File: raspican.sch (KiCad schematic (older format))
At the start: 17 parts, among them J2 CONN_01X06, P1 CONN_13X2, SW1 BUTTON_FRAME, SW2 BUTTON_FRAME, U4 MCP2515, Y1 16MHz

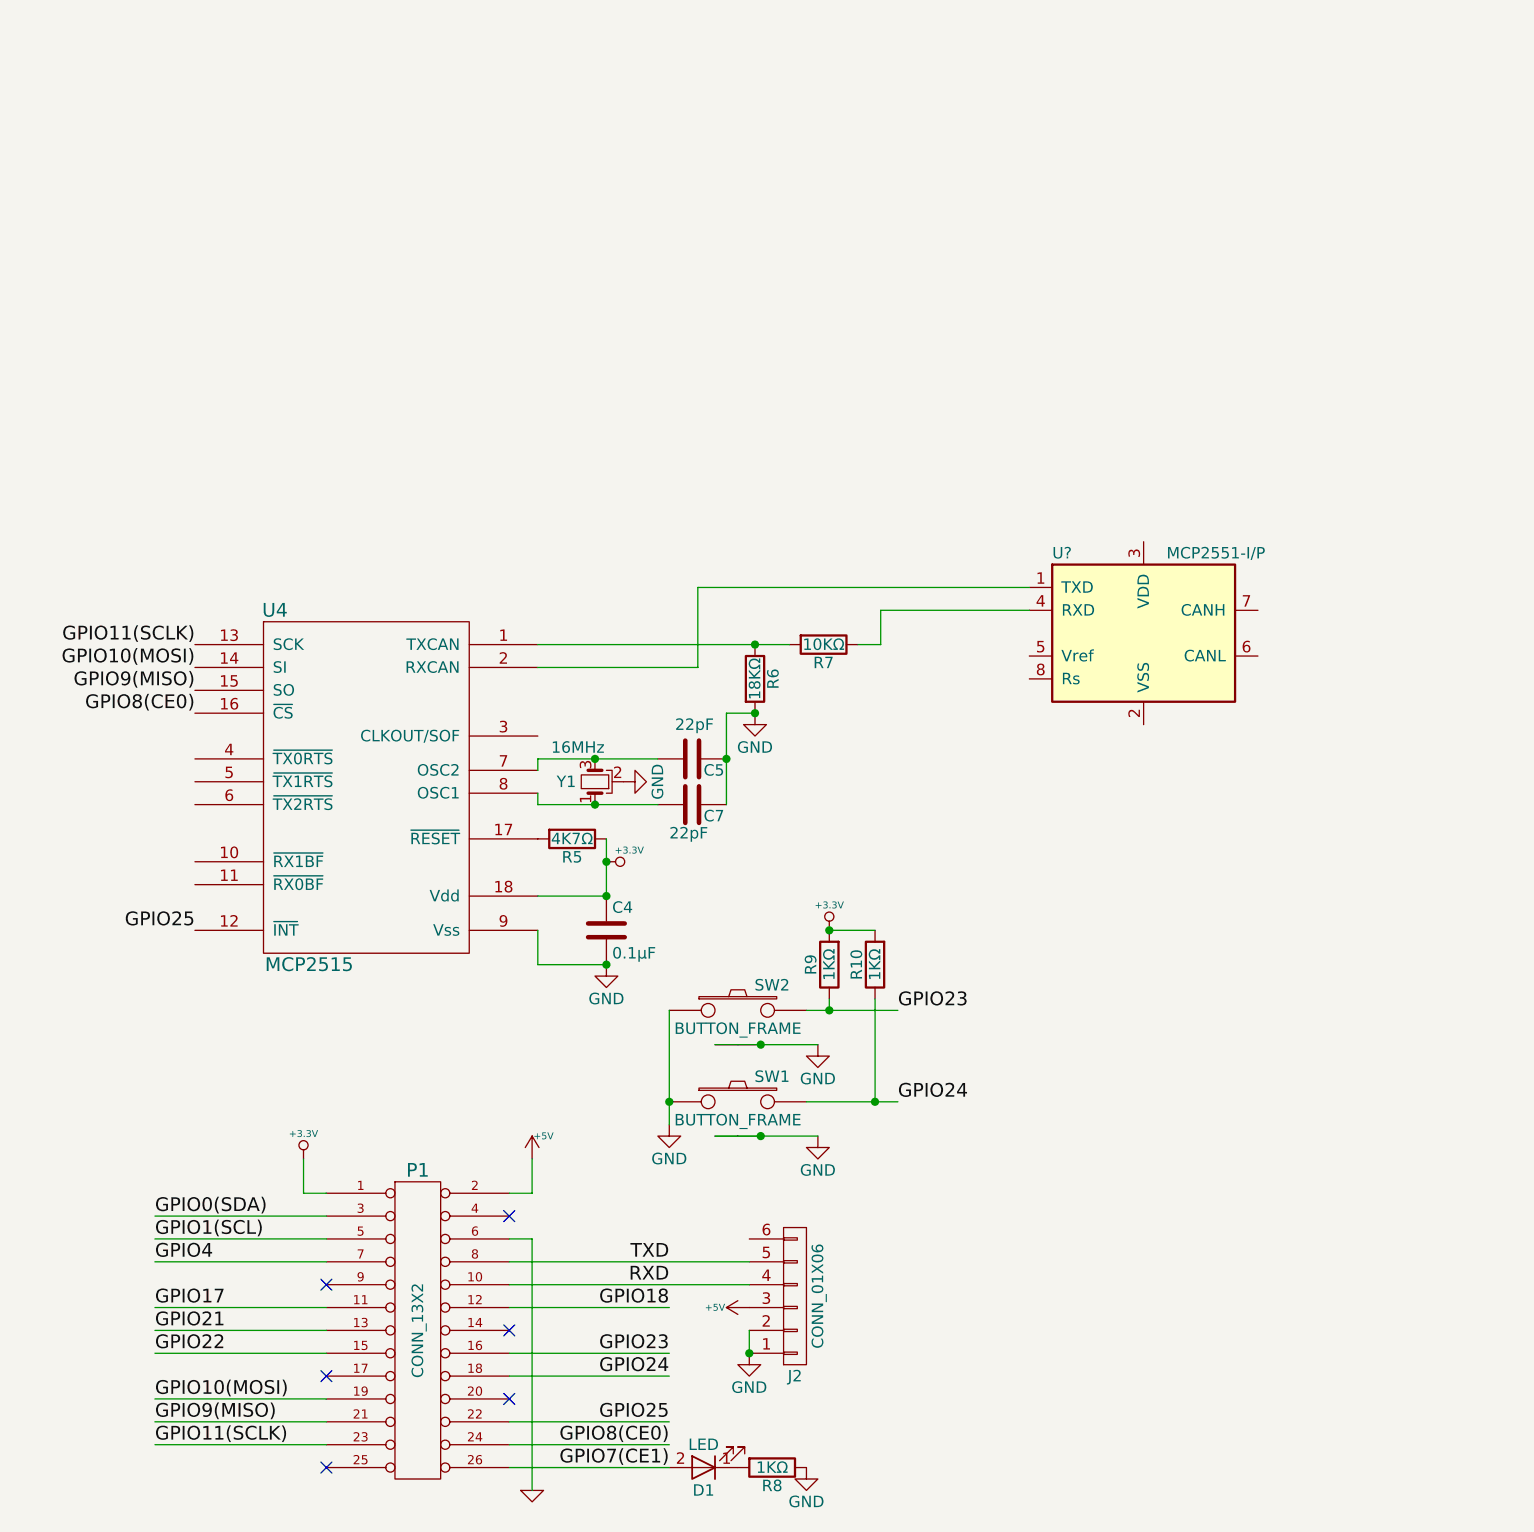
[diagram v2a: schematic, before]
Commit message: finished schematic, ready to make a board
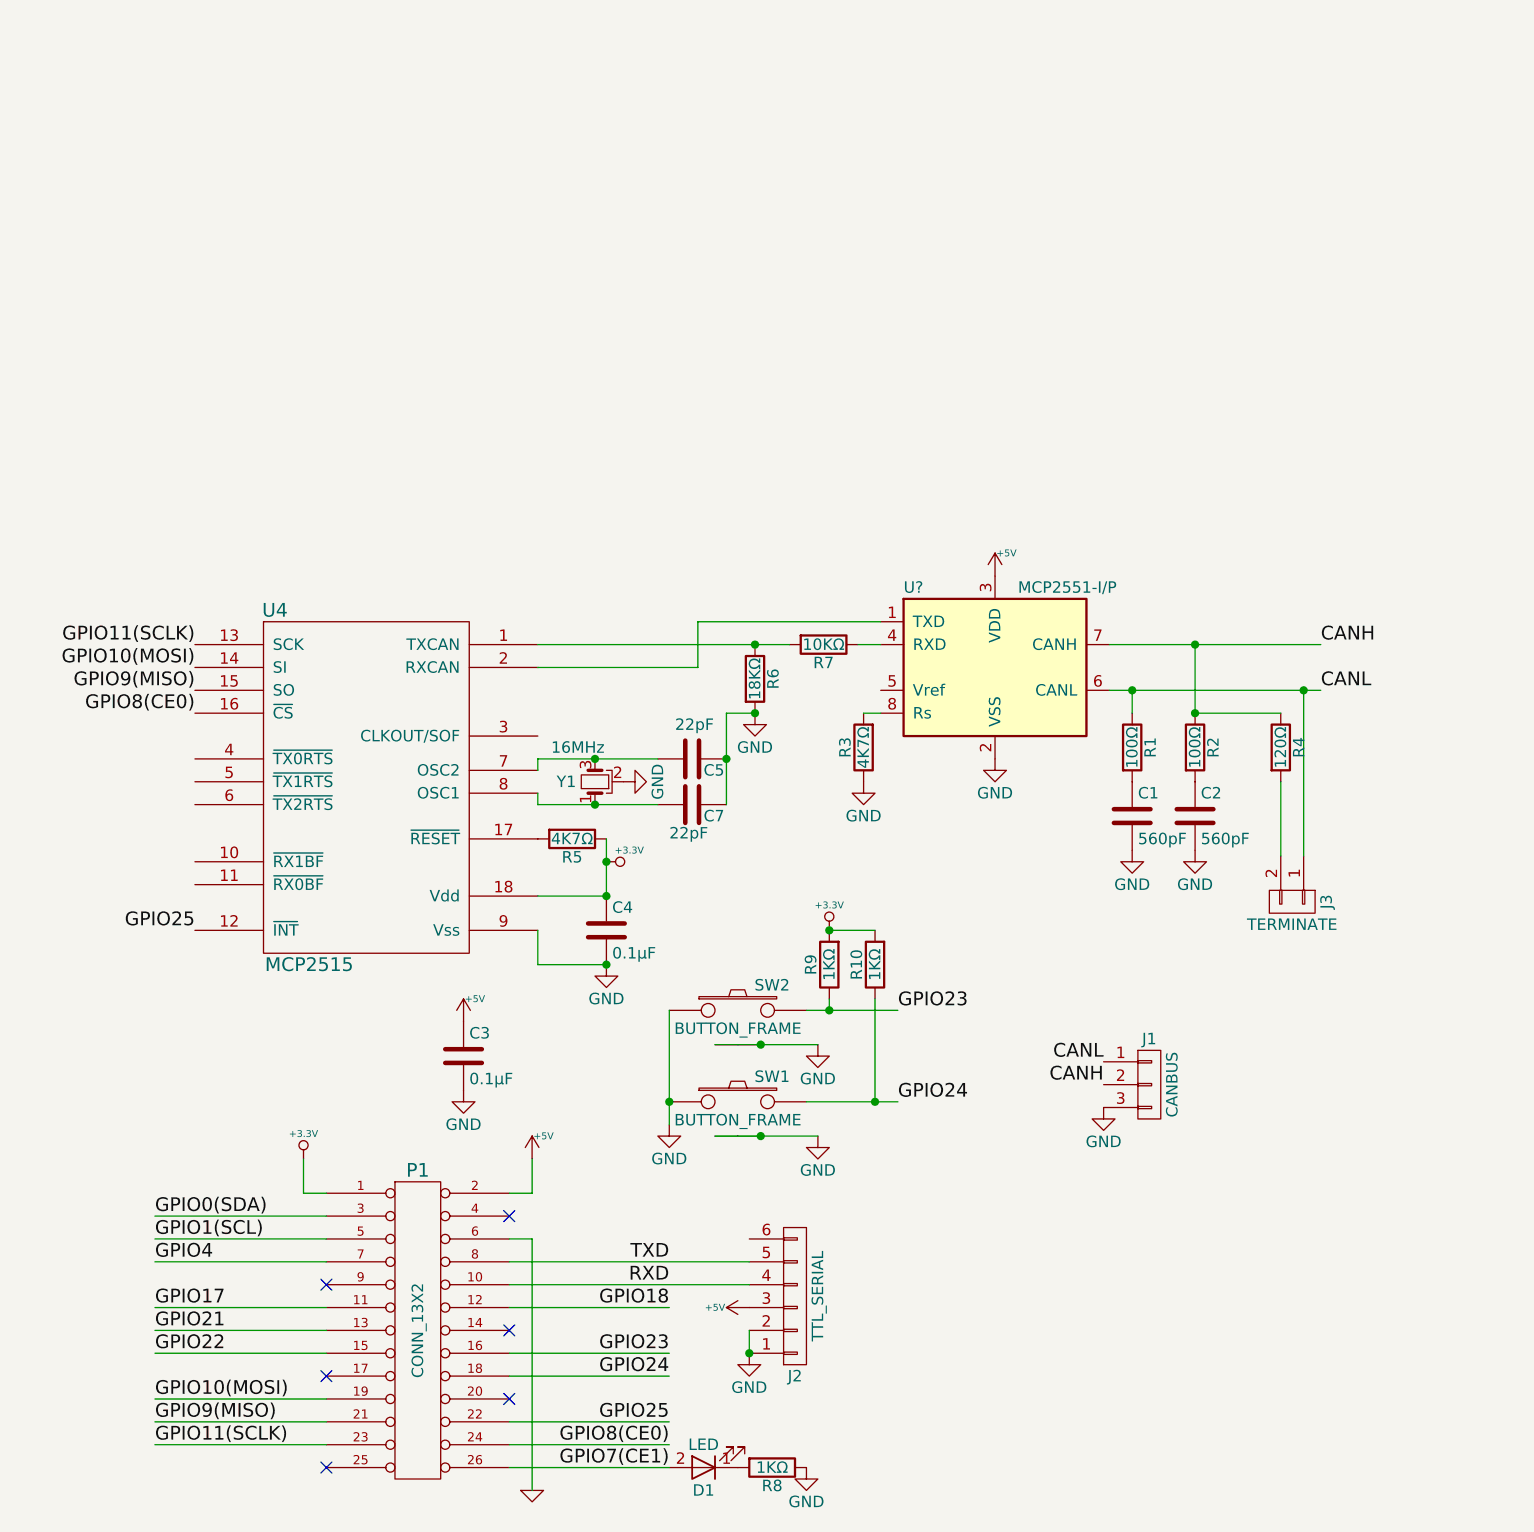
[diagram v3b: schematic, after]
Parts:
- added C1, C2: 560pF, symbol C
- added C3: 0.1μF, symbol C
- added J1: CANBUS, symbol CONN_01X03
- added J3: TERMINATE, symbol CONN_01X02
- added R1, R2: 100Ω, symbol R
- added R3: 4K7Ω, symbol R
- added R4: 120Ω, symbol R
- J2: value CONN_01X06 -> TTL_SERIAL
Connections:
- net +5V: now also U?.3 (VDD), C3.1
- net GND: now also U?.2 (VSS), C1.2, C2.2, C3.2, J1.3 (P3), R3.1
- net CANL: now reaches U?.6 (CANL)
- net CANL: now also J1.1 (P1), J3.1 (P1), R1.1
- net CANH: now reaches U?.7 (CANH)
- net CANH: now also J1.2 (P2), R2.1, R4.1
- net at U?.8 (Rs): now also R3.2
- new net: C1.1, R1.2
- new net: C2.1, R2.2
- new net: J3.2 (P2), R4.2
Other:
- moved on the sheet: U?
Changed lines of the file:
@@
 L MCP2551-I/P U?
 U 1 1 58B8BB6A
-P 5575 3600
-F 0 "U?" H 5175 3950 50  0000 L CNN
-F 1 "MCP2551-I/P" H 5675 3950 50  0000 L CNN
-F 2 "Housings_DIP:DIP-8_W7.62mm" H 5575 3100 50  0001 C CIN
-F 3 "" H 5575 3600 50  0001 C CNN
-	1    5575 3600
+P 4925 3750
+F 0 "U?" H 4525 4100 50  0000 L CNN
+F 1 "MCP2551-I/P" H 5025 4100 50  0000 L CNN
+F 2 "Housings_DIP:DIP-8_W7.62mm" H 4925 3250 50  0001 C CIN
+F 3 "" H 4925 3750 50  0001 C CNN
+	1    4925 3750
 	1    0    0    -1
 $EndComp
@@
 P 4050 6500
 F 0 "J2" H 4050 6850 50  0000 C CNN
-F 1 "CONN_01X06" V 4150 6500 50  0000 C CNN
+F 1 "TTL_SERIAL" V 4150 6500 50  0000 C CNN
 F 2 "" H 4050 6500 50  0001 C CNN
 F 3 "" H 4050 6500 50  0001 C CNN
@@
 Wire Wire Line
 	2925 3750 3625 3750
-Wire Wire Line
-	3625 3750 3625 3400
-Wire Wire Line
-	3625 3400 5075 3400
 $Comp
 L R R7
@@
 Wire Wire Line
 	4325 3650 4425 3650
-Wire Wire Line
-	4425 3650 4425 3500
-Wire Wire Line
-	4425 3500 5075 3500
 $Comp
 L R R6
@@
 Text Label 1425 3650 2    60   ~ 0
 GPIO11(SCLK)
+$Comp
+L +5V #PWR?
+U 1 1 58BA15CD
+P 4925 3350
+F 0 "#PWR?" H 4925 3440 20  0001 C CNN
+F 1 "+5V" H 4975 3450 30  0000 C CNN
+F 2 "" H 4925 3350 60  0001 C CNN
+F 3 "" H 4925 3350 60  0001 C CNN
+	1    4925 3350
+	1    0    0    -1
+$EndComp
+$Comp
+L C C3
+U 1 1 58BA1693
+P 2600 5450
+F 0 "C3" H 2625 5550 50  0000 L CNN
+F 1 "0.1μF" H 2625 5350 50  0000 L CNN
+F 2 "" H 2638 5300 50  0001 C CNN
+F 3 "" H 2600 5450 50  0001 C CNN
+	1    2600 5450
+	1    0    0    -1
+$EndComp
+$Comp
+L GND #PWR?
+U 1 1 58BA19FF
+P 2600 5600
+F 0 "#PWR?" H 2600 5350 50  0001 C CNN
+F 1 "GND" H 2600 5450 50  0000 C CNN
+F 2 "" H 2600 5600 50  0001 C CNN
+F 3 "" H 2600 5600 50  0001 C CNN
+	1    2600 5600
+	1    0    0    -1
+$EndComp
+$Comp
+L +5V #PWR?
+U 1 1 58BA1B7F
+P 2600 5300
+F 0 "#PWR?" H 2600 5390 20  0001 C CNN
+F 1 "+5V" H 2650 5400 30  0000 C CNN
+F 2 "" H 2600 5300 60  0001 C CNN
+F 3 "" H 2600 5300 60  0001 C CNN
+	1    2600 5300
+	1    0    0    -1
+$EndComp
+$Comp
+L GND #PWR?
+U 1 1 58BA1C71
+P 4925 4150
+F 0 "#PWR?" H 4925 3900 50  0001 C CNN
+F 1 "GND" H 4925 4000 50  0000 C CNN
+F 2 "" H 4925 4150 50  0001 C CNN
+F 3 "" H 4925 4150 50  0001 C CNN
+	1    4925 4150
+	1    0    0    -1
+$EndComp
+$Comp
+L R R3
+U 1 1 58BA1CB2
+P 4350 4100
+F 0 "R3" V 4430 4100 50  0000 C CNN
+F 1 "4K7Ω" V 4350 4100 50  0000 C CNN
+F 2 "" V 4280 4100 50  0001 C CNN
+F 3 "" H 4350 4100 50  0001 C CNN
+	1    4350 4100
+	-1   0    0    1
+$EndComp
+Wire Wire Line
+	4350 3950 4425 3950
+$Comp
+L GND #PWR?
+U 1 1 58BA1E42
+P 4350 4250
+F 0 "#PWR?" H 4350 4000 50  0001 C CNN
+F 1 "GND" H 4350 4100 50  0000 C CNN
+F 2 "" H 4350 4250 50  0001 C CNN
+F 3 "" H 4350 4250 50  0001 C CNN
+	1    4350 4250
+	1    0    0    -1
+$EndComp
+$Comp
+L R R1
+U 1 1 58BA1E7C
+P 5525 4100
+F 0 "R1" V 5605 4100 50  0000 C CNN
+F 1 "100Ω" V 5525 4100 50  0000 C CNN
+F 2 "" V 5455 4100 50  0001 C CNN
+F 3 "" H 5525 4100 50  0001 C CNN
+	1    5525 4100
+	1    0    0    -1
+$EndComp
+$Comp
+L R R2
+U 1 1 58BA1F70
+P 5800 4100
+F 0 "R2" V 5880 4100 50  0000 C CNN
+F 1 "100Ω" V 5800 4100 50  0000 C CNN
+F 2 "" V 5730 4100 50  0001 C CNN
+F 3 "" H 5800 4100 50  0001 C CNN
+	1    5800 4100
+	1    0    0    -1
+$EndComp
+$Comp
+L C C2
+U 1 1 58BA1FBE
+P 5800 4400
+F 0 "C2" H 5825 4500 50  0000 L CNN
+F 1 "560pF" H 5825 4300 50  0000 L CNN
+F 2 "" H 5838 4250 50  0001 C CNN
+F 3 "" H 5800 4400 50  0001 C CNN
+	1    5800 4400
+	1    0    0    -1
+$EndComp
+$Comp
+L C C1
+U 1 1 58BA204E
+P 5525 4400
+F 0 "C1" H 5550 4500 50  0000 L CNN
+F 1 "560pF" H 5550 4300 50  0000 L CNN
+F 2 "" H 5563 4250 50  0001 C CNN
+F 3 "" H 5525 4400 50  0001 C CNN
+	1    5525 4400
+	1    0    0    -1
+$EndComp
+$Comp
+L GND #PWR?
+U 1 1 58BA21C8
+P 5525 4550
+F 0 "#PWR?" H 5525 4300 50  0001 C CNN
+F 1 "GND" H 5525 4400 50  0000 C CNN
+F 2 "" H 5525 4550 50  0001 C CNN
+F 3 "" H 5525 4550 50  0001 C CNN
+	1    5525 4550
+	1    0    0    -1
+$EndComp
+$Comp
+L GND #PWR?
+U 1 1 58BA221F
+P 5800 4550
+F 0 "#PWR?" H 5800 4300 50  0001 C CNN
+F 1 "GND" H 5800 4400 50  0000 C CNN
+F 2 "" H 5800 4550 50  0001 C CNN
+F 3 "" H 5800 4550 50  0001 C CNN
+	1    5800 4550
+	1    0    0    -1
+$EndComp
+$Comp
+L R R4
+U 1 1 58BA226F
+P 6175 4100
+F 0 "R4" V 6255 4100 50  0000 C CNN
+F 1 "120Ω" V 6175 4100 50  0000 C CNN
+F 2 "" V 6105 4100 50  0001 C CNN
+F 3 "" H 6175 4100 50  0001 C CNN
+	1    6175 4100
+	1    0    0    -1
+$EndComp
+Wire Wire Line
+	5800 3950 6175 3950
+Wire Wire Line
+	5425 3850 6350 3850
+Wire Wire Line
+	5525 3850 5525 3950
+Wire Wire Line
+	5425 3650 6350 3650
+Wire Wire Line
+	5800 3650 5800 3950
+Connection ~ 5800 3950
+Text Label 6350 3850 0    60   ~ 0
+CANL
+Text Label 6350 3650 0    60   ~ 0
+CANH
+Connection ~ 5800 3650
+Connection ~ 5525 3850
+$Comp
+L CONN_01X02 J3
+U 1 1 58BA2B1E
+P 6225 4775
+F 0 "J3" H 6225 4925 50  0000 C CNN
+F 1 "TERMINATE" V 6325 4775 50  0000 C CNN
+F 2 "" H 6225 4775 50  0001 C CNN
+F 3 "" H 6225 4775 50  0001 C CNN
+	1    6225 4775
+	0    1    1    0
+$EndComp
+Wire Wire Line
+	6175 4575 6175 4250
+Wire Wire Line
+	6275 4575 6275 3850
+Connection ~ 6275 3850
+$Comp
+L CONN_01X03 J1
+U 1 1 58BA2E44
+P 5600 5575
+F 0 "J1" H 5600 5775 50  0000 C CNN
+F 1 "CANBUS" V 5700 5575 50  0000 C CNN
+F 2 "" H 5600 5575 50  0001 C CNN
+F 3 "" H 5600 5575 50  0001 C CNN
+	1    5600 5575
+	1    0    0    -1
+$EndComp
+Text Label 5400 5475 2    60   ~ 0
+CANL
+Text Label 5400 5575 2    60   ~ 0
+CANH
+$Comp
+L GND #PWR?
+U 1 1 58BA31BD
+P 5400 5675
+F 0 "#PWR?" H 5400 5425 50  0001 C CNN
+F 1 "GND" H 5400 5525 50  0000 C CNN
+F 2 "" H 5400 5675 50  0001 C CNN
+F 3 "" H 5400 5675 50  0001 C CNN
+	1    5400 5675
+	1    0    0    -1
+$EndComp
+Wire Wire Line
+	4425 3550 3625 3550
+Wire Wire Line
+	3625 3550 3625 3750
 $EndSCHEMATC

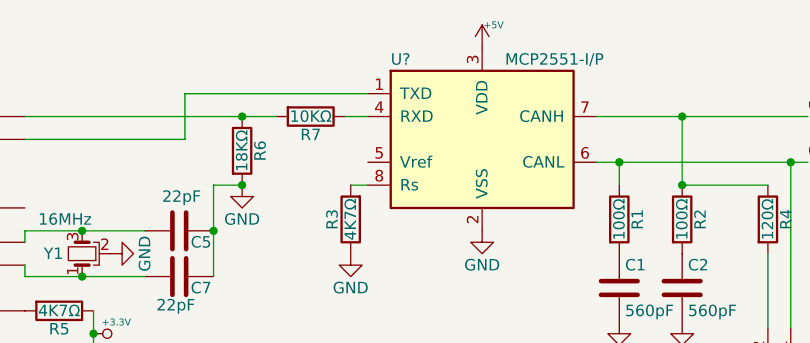
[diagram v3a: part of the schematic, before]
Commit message: assign through-hole footprints to all parts
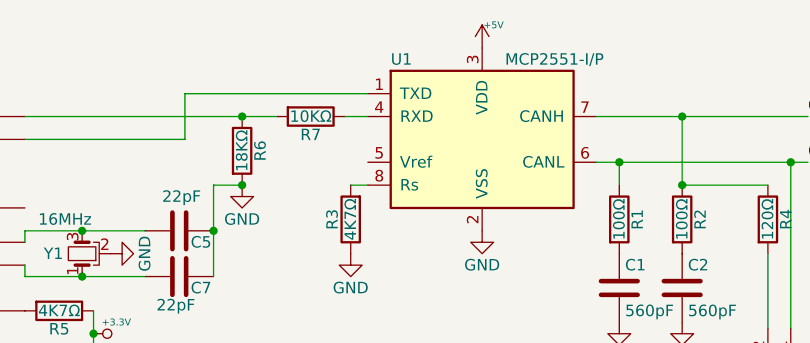
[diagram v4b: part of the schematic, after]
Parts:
- C1, C2, C3, C4, C5, C7: footprint (none) -> Capacitors_ThroughHole:C_Disc_D3_P2.5
- D1: footprint (none) -> LEDs:LED-5MM
- J1: footprint (none) -> Connectors_Phoenix:PhoenixContact_MSTBVA-G_03x5.08mm_Vertical
- J2: footprint (none) -> Pin_Headers:Pin_Header_Straight_1x06
- J3: footprint (none) -> Pin_Headers:Pin_Header_Straight_1x02
- P1: footprint (none) -> Pin_Headers:Pin_Header_Straight_2x13
- R1, R10, R2, R3, R4, R5, R6, R7, R8, R9: footprint (none) -> Resistors_ThroughHole:Resistor_Horizontal_RM10mm
- SW1, SW2: footprint (none) -> Buttons_Switches_ThroughHole:SW_Tactile_SPST_Angled
- U1: renamed from U?; footprint Housings_DIP:DIP-8_W7.62mm -> Housings_DIP:DIP-8_W7.62mm_LongPads
- U4: footprint (none) -> Housings_DIP:DIP-18_W7.62mm_LongPads
- Y1: footprint (none) -> Crystals:Crystal_HC49-U_Vertical_3Pin

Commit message: change crystal in schematic to have ground on pin 3
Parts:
- Y1: symbol Crystal_GND2_Small -> Crystal_GND3
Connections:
- net GND: now also Y1.3; no longer Y1.2
- net at C5.2, U4.7 (OSC2): now also Y1.2; no longer Y1.3
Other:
- moved on the sheet: C5, C7
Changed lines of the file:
@@
 Connection ~ 3225 5050
 $Comp
-L Crystal_GND2_Small Y1
+L Crystal_GND3 Y1
 U 1 1 58BA01F9
-P 3175 4250
-F 0 "Y1" V 3175 4375 50  0000 C CNN
-F 1 "16MHz" V 3325 4325 50  0000 C CNN
-F 2 "Crystals:Crystal_HC49-U_Vertical_3Pin" H 3175 4250 50  0001 C CNN
-F 3 "" H 3175 4250 50  0001 C CNN
-	1    3175 4250
+P 3100 4250
+F 0 "Y1" V 3100 4250 50  0000 C CNN
+F 1 "16MHz" V 3300 4250 50  0000 C CNN
+F 2 "Crystals:Crystal_HC49-U_Vertical_3Pin" H 3100 4250 50  0001 C CNN
+F 3 "" H 3100 4250 50  0001 C CNN
+	1    3100 4250
 	0    -1   -1   0
 $EndComp
 Wire Wire Line
-	2925 4150 3450 4150
+	2925 4100 3450 4100
 Wire Wire Line
-	2925 4150 2925 4200
+	2925 4100 2925 4200
 Wire Wire Line
-	2925 4300 2925 4350
+	2925 4300 2925 4400
 Wire Wire Line
-	2925 4350 3450 4350
+	2925 4400 3450 4400
 $Comp
 L GND #PWR014
@@
 L C C5
 U 1 1 58BA0567
-P 3600 4150
-F 0 "C5" V 3650 4200 50  0000 L CNN
-F 1 "22pF" V 3450 4075 50  0000 L CNN
-F 2 "Capacitors_ThroughHole:C_Disc_D3_P2.5" H 3638 4000 50  0001 C CNN
-F 3 "" H 3600 4150 50  0001 C CNN
-	1    3600 4150
+P 3600 4100
+F 0 "C5" V 3650 4150 50  0000 L CNN
+F 1 "22pF" V 3450 4025 50  0000 L CNN
+F 2 "Capacitors_ThroughHole:C_Disc_D3_P2.5" H 3638 3950 50  0001 C CNN
+F 3 "" H 3600 4100 50  0001 C CNN
+	1    3600 4100
 	0    1    1    0
 $EndComp
@@
 L C C7
 U 1 1 58BA05DB
-P 3600 4350
-F 0 "C7" V 3650 4400 50  0000 L CNN
-F 1 "22pF" V 3725 4250 50  0000 L CNN
-F 2 "Capacitors_ThroughHole:C_Disc_D3_P2.5" H 3638 4200 50  0001 C CNN
-F 3 "" H 3600 4350 50  0001 C CNN
-	1    3600 4350
+P 3600 4400
+F 0 "C7" V 3650 4450 50  0000 L CNN
+F 1 "22pF" V 3725 4300 50  0000 L CNN
+F 2 "Capacitors_ThroughHole:C_Disc_D3_P2.5" H 3638 4250 50  0001 C CNN
+F 3 "" H 3600 4400 50  0001 C CNN
+	1    3600 4400
 	0    1    1    0
 $EndComp
 Wire Wire Line
-	3750 3950 3750 4350
+	3750 3950 3750 4400
 Wire Wire Line
 	3750 3950 3875 3950
-Connection ~ 3750 4150
+Connection ~ 3750 4100
 Connection ~ 3875 3950
-Connection ~ 3175 4150
-Connection ~ 3175 4350
+Connection ~ 3100 4100
+Connection ~ 3100 4400
 Text Label 1425 3950 2    60   ~ 0
 GPIO8(CE0)
